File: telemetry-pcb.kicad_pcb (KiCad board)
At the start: 2 copper layers, 150 x 130 mm, 64 parts, among them CN1 12V_IN, CN10 CAN, CN11 CAN, CN12 CAN_12V_OUT, CN13 THERMO1, CN14 THERMO2, CN15 RS232, CN2 12V_OUT, CN3 12V_OUT, CN4 12V_OUT, CN5 12V_OUT, CN6 CAN, CN7 CAN, CN8 CAN, CN9 CAN, IC1 MAX31855K, IC2 MAX31855K, IC3 TCAN332DR, IC4 MAX3232CPWR, IC5 MCP2515-xSO, M1 MountingHole, M2 MountingHole, M3 MountingHole, M4 MountingHole, T1 TEST_12V, T2 TEST_3V3, T3 TEST_CAN, T4 GPIO_L, T5 GPIO_R, T6 TEST_RS232, Y1 8MHz

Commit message: small changes and gerber file for JLPCB
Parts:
- H1,H2: renamed from H1                  H2
- R3: value 68 -> 5.6
- R4: value 4.7 -> 5.6
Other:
- board text added: "12V"
- board text added: "2021-09-08"
- board text added: "Telemetry Module v1.0"

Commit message: added JLPCB gerber files
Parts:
- added G***: LOGO, Libraries:sm_logo, B.Cu at (80.0, 104.2)

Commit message: started on 1.1 redesign, schematic is done and PCB has just been started.
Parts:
- removed G***: LOGO, Libraries:sm_logo
- removed S2: AUX_BTN_1, TestPoint:TestPoint_2Pads_Pitch2.54mm_Drill0.8mm
- removed S4: AUX_BTN_3, TestPoint:TestPoint_2Pads_Pitch2.54mm_Drill0.8mm
- added C16: 0.1uF, Capacitor_SMD:C_0805_2012Metric, B.Cu at (-3.51, -37.9)
- added IC6: LSM6DSOTR, telemetry-pcb:LSM6DSOTR, B.Cu at (-24.7, -40.2)
- added J1: TTL, telemetry-pcb:molex_sl_1x04_horizontal, F.Cu at (63.3, 84.4)
- added R7: 120, Resistor_SMD:R_0805_2012Metric, B.Cu at (-21.6, 5.97)
- added R8: 10K, Resistor_SMD:R_0805_2012Metric, B.Cu at (1.41, -34.4)
- C1: value 0.1uF -> 47uF; footprint Capacitor_SMD:C_0805_2012Metric -> Capacitor_SMD:CP_Elec_6.3x5.4
- C10, C9: value 0.01uF -> 0.1uF; moved to B.Cu
- C11, C12, C15, C2, C3, C4, C5, C6, D1, IC2, R1, R3, R4, R5, R6: moved to B.Cu
- C13: value 10uF -> 0.1uF; footprint Capacitor_SMD:C_1206_3216Metric -> Capacitor_SMD:C_0805_2012Metric; moved to B.Cu
- C14: value 47uF -> 10uF; footprint Capacitor_SMD:CP_Elec_6.3x5.4 -> Capacitor_SMD:C_1206_3216Metric; moved to B.Cu
- C7, C8: value 0.1uF -> 0.01uF; moved to B.Cu
- CN1: value 12V_IN -> 12V_OUT; footprint Connector_Molex:Molex_Mega-Fit_76825-0004_2x02_P5.70mm_Horizontal -> Connector_Molex:Molex_Mega-Fit_76825-0004_1x02_P5.70mm_Horizontal
- CN10, CN11, CN6, CN8, CN9: footprint Conn_Molex_70553-0001:Molex-70553-0001-0-0-MFG -> telemetry-pcb:molex_sl_1x02_horizontal
- CN12: value CAN_12V_OUT -> CAN; footprint Connector_Molex:Molex_Mega-Fit_76825-0010_2x05_P5.70mm_Horizontal -> telemetry-pcb:molex_sl_1x02_horizontal
- CN13: value THERMO1 -> RS232; footprint Conn_Molex_70553-0002:Molex-70551-0002-0-0-0 -> telemetry-pcb:db-9
- CN14: value THERMO2 -> THERMO1; footprint Conn_Molex_70553-0002:Molex-70551-0002-0-0-0 -> telemetry-pcb:molex-sl-1x03-horizontal
- CN15: value RS232 -> THERMO2; footprint Libraries:DLS1XP5AK40X -> telemetry-pcb:molex-sl-1x03-horizontal
- CN2: value 12V_OUT -> 12V_IN; footprint Connector_Molex:Molex_Mega-Fit_76825-0004_1x02_P5.70mm_Horizontal -> Connector_Molex:Molex_Mega-Fit_76825-0004_2x02_P5.70mm_Horizontal
- CN7: value CAN -> CAN_12V_OUT; footprint Conn_Molex_70553-0001:Molex-70553-0001-0-0-MFG -> Connector_Molex:Molex_Mega-Fit_76825-0010_2x05_P5.70mm_Horizontal
- H1,H2: footprint Libraries:PCB_FeatherWing -> telemetry-pcb:Particle_boron
- IC1: value MAX31855K -> MAX3232CPWR; footprint Package_SO:SOIC-8-1EP_3.9x4.9mm_P1.27mm_EP2.29x3mm -> Package_SO:TSSOP-16_4.4x5mm_P0.65mm; moved to B.Cu
- IC3: value TCAN332DR -> MAX31855K; footprint Libraries:SOIC127P599X175-8N -> Package_SO:SOIC-8-1EP_3.9x4.9mm_P1.27mm_EP2.29x3mm; moved to B.Cu
- IC4: value MAX3232CPWR -> MCP2515-xSO; footprint Package_SO:TSSOP-16_4.4x5mm_P0.65mm -> Package_SO:SOIC-18W_7.5x11.6mm_P1.27mm; moved to B.Cu
- IC5: value MCP2515-xSO -> TCAN332DR; footprint Package_SO:SOIC-18W_7.5x11.6mm_P1.27mm -> Package_SO:SOIC-8-1EP_3.9x4.9mm_P1.27mm_EP2.29x3mm; moved to B.Cu
- R2: value 10K -> 120; moved to B.Cu
- S3: value AUX_BTN_2 -> LOG_BTN
- T1: value TEST_12V -> TEST_3V3
- T2: value TEST_3V3 -> TEST_12V
- moved C14 260.8 mm to (-30.5, -39.8), turned to 0 degrees
- moved D1 238.8 mm to (-36.1, -8.99), turned to 0 degrees
- moved R6 226.9 mm to (-21.6, 3.02)
- moved C9 225.4 mm to (-20.0, -39.8), turned to 0 degrees
- moved R3 224.5 mm to (-21.5, -19.3), turned to 0 degrees
- moved R4 223.1 mm to (-25.9, -19.3), turned to 0 degrees
- moved R5 204.1 mm to (-12.6, -16.3), turned to 0 degrees
- moved IC1 202.3 mm to (-11.7, -6.25), turned to 0 degrees
- moved C10 197.1 mm to (-15.5, -39.8), turned to 0 degrees
- moved C12 195.2 mm to (-11.1, -40.9), turned to 0 degrees
- moved C2 193.8 mm to (3.90, -4.46), turned to 0 degrees
- moved C11 184.6 mm to (-7.96, -37.9), turned to 0 degrees
- moved IC2 175.5 mm to (7.89, -20.0), turned to 0 degrees
- moved C5 171.5 mm to (-9.45, -11.0), turned to 0 degrees
- moved C6 170.9 mm to (-13.9, -11.0)
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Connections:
- C1 pad 1: +3V3 -> /VIN
- C10 pad 1: Net-(C10-Pad1) -> +3V3
- C10 pad 2: Net-(C10-Pad2) -> GND
- C13 pad 1: +3V3 -> GND
- C13 pad 2: GND -> +3V3
- C14 pad 1: /VIN -> +3V3
- C15 pad 1: GND -> +3V3
- C15 pad 2: +3V3 -> GND
- C2 pad 1: +3V3 -> Net-(C2-Pad1)
- C2 pad 2: GND -> Net-(C2-Pad2)
- C3 pad 2: GND -> Net-(C3-Pad2)
- C4 pad 1: GND -> Net-(C4-Pad1)
- C4 pad 2: Net-(C4-Pad2) -> GND
- C5 pad 1: Net-(C5-Pad1) -> GND
- C5 pad 2: Net-(C5-Pad2) -> +3V3
- C6 pad 1: Net-(C6-Pad1) -> GND
- C7 pad 1: GND -> Net-(C7-Pad1)
- C7 pad 2: +3V3 -> Net-(C7-Pad2)
- C8 pad 1: GND -> Net-(C8-Pad1)
- C8 pad 2: +3V3 -> Net-(C8-Pad2)
- C9 pad 1: Net-(C9-Pad1) -> +3V3
- C9 pad 2: Net-(C9-Pad2) -> GND
- CN1 pad 2: GND -> +12V
- CN10 pad 1: /CANL -> /Power & CAN Distribution/CANL
- CN10 pad 2: /CANH -> /Power & CAN Distribution/CANH
- CN11 pad 1: /CANL -> /Power & CAN Distribution/CANL
- CN11 pad 2: /CANH -> /Power & CAN Distribution/CANH
- CN12 pad 1: GND -> /Power & CAN Distribution/CANL
- CN12 pad 2: GND -> /Power & CAN Distribution/CANH
- CN13 pad 1: Net-(C9-Pad2) -> Net-(CN13-Pad1)
- CN13 pad 3: Net-(C9-Pad1) -> Net-(CN13-Pad3)
- CN14 pad 1: Net-(C10-Pad2) -> Net-(C7-Pad2)
- CN14 pad 3: Net-(C10-Pad1) -> Net-(C7-Pad1)
- CN15 pad 1: Net-(CN15-Pad1) -> Net-(C8-Pad2)
- CN15 pad 3: Net-(CN15-Pad3) -> Net-(C8-Pad1)
- CN2 pad 2: +12V -> GND
- CN6 pad 1: /CANL -> /Power & CAN Distribution/CANL
- CN6 pad 2: /CANH -> /Power & CAN Distribution/CANH
- CN7 pad 1: /CANL -> GND
- CN7 pad 2: /CANH -> GND
- CN8 pad 1: /CANL -> /Power & CAN Distribution/CANL
- CN8 pad 2: /CANH -> /Power & CAN Distribution/CANH
- CN9 pad 1: /CANL -> /Power & CAN Distribution/CANL
- CN9 pad 2: /CANH -> /Power & CAN Distribution/CANH
- F1 pad 1: Net-(CN1-Pad3) -> Net-(CN2-Pad3)
- IC1 pad 1: GND -> Net-(C2-Pad1)
- IC1 pad 2: Net-(C9-Pad1) -> Net-(C6-Pad2)
- IC1 pad 3: Net-(C9-Pad2) -> Net-(C2-Pad2)
- IC1 pad 4: +3V3 -> Net-(C3-Pad2)
- IC1 pad 5: /SCK -> Net-(C3-Pad1)
- IC1 pad 6: /A5 -> Net-(C4-Pad1)
- IC1 pad 7: /MI -> Net-(IC1-Pad7)
- IC1 pad 8: (no net) -> Net-(IC1-Pad8)
- IC1 pad 9: (no net) -> Net-(IC1-Pad9)
- IC2 pad 2: Net-(C10-Pad1) -> Net-(C7-Pad1)
- IC2 pad 3: Net-(C10-Pad2) -> Net-(C7-Pad2)
- IC2 pad 5: /SCK -> /MO
- IC2 pad 6: /A4 -> /A5
- IC3 pad 1: Net-(IC3-Pad1) -> GND
- IC3 pad 2: GND -> Net-(C8-Pad1)
- IC3 pad 3: +3V3 -> Net-(C8-Pad2)
- IC3 pad 4: Net-(IC3-Pad4) -> +3V3
- IC3 pad 5: (no net) -> /MO
- IC3 pad 6: /CANL -> /A4
- IC3 pad 7: /CANH -> /MI
- IC4 pad 1: Net-(C6-Pad1) -> Net-(IC4-Pad1)
- IC4 pad 11: /TX -> Net-(IC4-Pad11)
- IC4 pad 12: /RX -> /D6
- IC4 pad 13: Net-(CN15-Pad3) -> /SCK1
- IC4 pad 14: Net-(CN15-Pad2) -> /MO1
- IC4 pad 15: GND -> /MI1
- IC4 pad 16: +3V3 -> /D5
- IC4 pad 2: Net-(C4-Pad2) -> Net-(IC4-Pad2)
- IC4 pad 3: Net-(C6-Pad2) -> Net-(IC4-Pad3)
- IC4 pad 4: Net-(C5-Pad2) -> Net-(IC4-Pad4)
- IC4 pad 5: Net-(C5-Pad1) -> Net-(IC4-Pad5)
- IC4 pad 6: Net-(C3-Pad1) -> Net-(IC4-Pad6)
- IC4 pad 7: Net-(IC4-Pad7) -> Net-(C11-Pad1)
- IC4 pad 8: Net-(IC4-Pad8) -> Net-(C12-Pad1)
- IC4 pad 9: Net-(IC4-Pad9) -> GND
- IC5 pad 1: Net-(IC3-Pad1) -> Net-(IC4-Pad1)
- IC5 pad 2: Net-(IC3-Pad4) -> GND
- IC5 pad 3: Net-(IC5-Pad3) -> +3V3
- IC5 pad 4: Net-(IC5-Pad4) -> Net-(IC4-Pad2)
- IC5 pad 5: Net-(IC5-Pad5) -> (no net)
- IC5 pad 6: Net-(IC5-Pad6) -> /Power & CAN Distribution/CANL
- IC5 pad 7: Net-(C11-Pad1) -> /Power & CAN Distribution/CANH
- IC5 pad 8: Net-(C12-Pad1) -> (no net)
- IC5 pad 9: GND -> (no net)
- R1 pad 1: Net-(R1-Pad1) -> GND
- R1 pad 2: /CANL -> /A1
- R2 pad 1: Net-(IC5-Pad17) -> /A1
- R2 pad 2: +3V3 -> /VIN
- R5 pad 1: /A0 -> Net-(L4-Pad2)
- R5 pad 2: Net-(L4-Pad2) -> /A0
- R6 pad 1: /VIN -> Net-(L1-Pad2)
- R6 pad 2: Net-(L1-Pad2) -> +12V
- S1 pad 1: /CANH -> Net-(R7-Pad1)
- S1 pad 2: Net-(R1-Pad1) -> /Power & CAN Distribution/CANL
- T1 pad 1: +12V -> +3V3
- T2 pad 1: +3V3 -> +12V
- T3 pad 1: /CANL -> /Power & CAN Distribution/CANL
- T3 pad 2: /CANH -> /Power & CAN Distribution/CANH
- T6 pad 1: Net-(CN15-Pad2) -> Net-(CN13-Pad2)
- T6 pad 2: Net-(CN15-Pad3) -> Net-(CN13-Pad3)
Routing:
- net +3V3: track 241.1 -> 0.00 mm, vias 8 -> 0
- net /CANH: track 201.2 -> 0.00 mm, vias 3 -> 0
- net /CANL: track 193.6 -> 0.00 mm, vias 2 -> 0
- net GND: track 160.7 -> 0.00 mm, vias 4 -> 0
- net /SDA: track 120.5 -> 0.00 mm
- net /SCL: track 114.5 -> 0.00 mm, vias 1 -> 0
- net /A3: track 99.6 -> 0.00 mm
- net /A2: track 96.1 -> 0.00 mm
- net /A1: track 92.5 -> 0.00 mm
- net /D6: track 66.3 -> 0.00 mm, vias 1 -> 0
- net /D5: track 56.3 -> 0.00 mm
- net /MI1: track 53.2 -> 0.00 mm
- net /MO1: track 50.1 -> 0.00 mm
- net Net-(L2-Pad2): track 49.1 -> 0.00 mm
- net /A0: track 47.8 -> 0.00 mm
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- removed copper zone on F.Cu, net +12V
- removed copper zone on B.Cu, net GND
- removed copper zone on F.Cu, net GND
- removed copper zone on F.Cu, net Net-(CN1-Pad3)
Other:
- board size 150 x 130 mm -> 150 x 100 mm
- board text removed: "12V"
- board text removed: "12V+"
- board text removed: "12V_OUT"
- board text removed: "2021-09-08"
- board text removed: "3V3"
- board text removed: "CAN"
- board text removed: "CELL ANTENNA"
- board text removed: "GND"
- board text removed: "H"
- board text removed: "L"
- board text removed: "RX"
- board text removed: "TX"
- board text removed: "Telemetry Module v1.0"

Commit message: finished schematic and PCB layout for 1.1 board
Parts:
- removed CN10, CN11, CN12, CN9: CAN, telemetry-pcb:molex_sl_1x02_horizontal
- removed the CN3 at (123.7, 103.7)
- removed the CN5 at (159.3, 103.7)
- removed the CN6 at (65.3, 27.0)
- removed the R6 at (-21.6, 3.02)
- removed S3: LOG_BTN, TestPoint:TestPoint_2Pads_Pitch2.54mm_Drill0.8mm
- removed the T2 at (148.6, 81.3)
- removed the T3 at (114.1, 40.7)
- added J2: Header 02x03, Connector_PinHeader_2.54mm:PinHeader_2x03_P2.54mm_Horizontal, F.Cu at (82.6, 80.8)
- added Q1: IF-D92, telemetry-pcb:IF-D92, F.Cu at (173.5, 66.6)
- added R3: 10K, Resistor_SMD:R_0805_2012Metric, B.Cu at (186.7, 98.6)
- added R9: 120, Resistor_SMD:R_0805_2012Metric, B.Cu at (133.4, 108.8)
- added S2: CAN_TERM, Button_Switch_THT:SW_DIP_SPSTx01_Piano_10.8x4.1mm_W7.62mm_P2.54mm, F.Cu at (135.9, 121.0)
- added T1: TEST_12V, TestPoint:TestPoint_2Pads_Pitch2.54mm_Drill0.8mm, F.Cu at (76.0, 109.3)
- added T6: TEST_CAN, TestPoint:TestPoint_2Pads_Pitch2.54mm_Drill0.8mm, F.Cu at (73.4, 114.4)
- CN1: value 12V_OUT -> 12V; footprint Connector_Molex:Molex_Mega-Fit_76825-0004_1x02_P5.70mm_Horizontal -> telemetry-pcb:molex_sl_1x04_horizontal
- CN2: value 12V_IN -> 12V; footprint Connector_Molex:Molex_Mega-Fit_76825-0004_2x02_P5.70mm_Horizontal -> telemetry-pcb:molex_sl_1x04_horizontal
- CN4: value 12V_OUT -> UART; footprint Connector_Molex:Molex_Mega-Fit_76825-0004_1x02_P5.70mm_Horizontal -> telemetry-pcb:Molex-70551-0004-0
- CN7: value CAN_12V_OUT -> CAN; footprint Connector_Molex:Molex_Mega-Fit_76825-0010_2x05_P5.70mm_Horizontal -> telemetry-pcb:molex_sl_1x02_horizontal
- D1: value 1A 50v -> 2A 50v; moved to F.Cu
- F1: value 25A -> 1A; footprint Fuse:Fuseholder_Blade_Mini_Keystone_3568 -> telemetry-pcb:0154001.DRL
- G1: renamed from H3; footprint Connector_PinSocket_2.54mm:PinSocket_1x08_P2.54mm_Vertical -> telemetry-pcb:Sparkfun GPS
- J1: value TTL -> Header 02x02; footprint telemetry-pcb:molex_sl_1x04_horizontal -> Connector_PinHeader_2.54mm:PinHeader_2x02_P2.54mm_Horizontal
- R1: value 120 -> 2.2K
- R2: value 120 -> 560
- R4: renamed from R5; moved to F.Cu
- R5: renamed from R4; moved to F.Cu
- R6: renamed from R3; moved to F.Cu
- R7: value 120 -> 10K
- S1: value CAN_TERM -> LOG; footprint Button_Switch_THT:SW_DIP_SPSTx01_Piano_10.8x4.1mm_W7.62mm_P2.54mm -> Button_Switch_THT:SW_PUSH_6mm_H13mm
- moved C14 253.8 mm to (176.0, 107.8), turned to 90 degrees
- moved C13 222.2 mm to (181.6, 108.3), turned to 270 degrees
- moved R1 221.0 mm to (181.6, 98.6), turned to 90 degrees
- moved R8 220.7 mm to (175.5, 101.2), turned to 270 degrees
- moved IC6 220.2 mm to (144.6, 100.6)
- moved C11 217.6 mm to (153.7, 107.8), turned to 90 degrees
- moved C12 217.2 mm to (153.7, 100.6), turned to 270 degrees
- moved R7 213.3 mm to (182.1, 69.2)
- moved C15 212.1 mm to (147.6, 104.7)
- moved IC4 211.9 mm to (166.4, 104.2)
- moved D1 206.1 mm to (137.4, 102.2), turned to 180 degrees
- moved R6 202.2 mm to (157.8, 74.2), turned to 90 degrees
- moved R5 201.2 mm to (152.2, 74.2), turned to 270 degrees
- moved IC5 195.1 mm to (121.2, 105.2), turned to 180 degrees
- moved C16 193.4 mm to (128.8, 103.2), turned to 270 degrees
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- renumbered CN13 to CN3, CN14 to CN5, CN15 to CN6, H1,H2 to H1, L4 to L2, L2 to L4, T4 to T2, T5 to T3, T1 to T4, T6 to T5
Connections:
- CN1 pad 2: +12V -> GND
- CN2 pad 3: Net-(CN2-Pad3) -> Net-(CN1-Pad3)
- CN2 pad 4: Net-(CN2-Pad3) -> Net-(CN1-Pad3)
- CN3 pad 5: Net-(CN13-Pad5) -> GND
- CN4 pad 2: +12V -> Net-(CN4-Pad2)
- CN7 pad 1: GND -> Net-(CN7-Pad1)
- CN7 pad 2: GND -> Net-(CN7-Pad2)
- CN8 pad 1: /Power & CAN Distribution/CANL -> Net-(CN7-Pad1)
- CN8 pad 2: /Power & CAN Distribution/CANH -> Net-(CN7-Pad2)
- D1 pad 2: +12V -> Net-(D1-Pad2)
- F1 pad 1: Net-(CN2-Pad3) -> Net-(CN1-Pad3)
- F1 pad 2: +12V -> Net-(D1-Pad2)
- IC1 pad 11: /TX -> Net-(IC1-Pad11)
- IC1 pad 12: /RX -> Net-(IC1-Pad12)
- IC2 pad 5: /MO -> /SCK
- IC3 pad 5: /MO -> /SCK
- IC5 pad 6: /Power & CAN Distribution/CANL -> Net-(CN7-Pad1)
- IC5 pad 7: /Power & CAN Distribution/CANH -> Net-(CN7-Pad2)
- IC6 pad 13: /MO -> /SCK
- IC6 pad 14: /SCK -> /MO
- J1 pad 1: /TX -> Net-(IC1-Pad11)
- J1 pad 3: /RX -> Net-(CN4-Pad4)
- J1 pad 4: /RX -> /TX
- R2 pad 1: /A1 -> Net-(D1-Pad2)
- R2 pad 2: /VIN -> Net-(L1-Pad2)
- R7 pad 1: Net-(R7-Pad1) -> Net-(Q1-Pad2)
- R7 pad 2: /Power & CAN Distribution/CANH -> GND
- S1 pad 1: Net-(R7-Pad1) -> GND
- S1 pad 2: /Power & CAN Distribution/CANL -> /A2
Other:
- board size 150 x 100 mm -> 120 x 70 mm

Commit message: routed all
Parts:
- R2: moved to F.Cu
- T2: footprint Connector_PinSocket_2.54mm:PinSocket_1x15_P2.54mm_Vertical -> telemetry-pcb:Boron_Pins_L
- T3: footprint Connector_PinSocket_2.54mm:PinSocket_1x12_P2.54mm_Vertical -> telemetry-pcb:Boron_Pins_R
- moved C1 17.3 mm to (135.4, 101.7)
- moved R2 16.1 mm to (127.3, 74.7), turned to 270 degrees
- moved D1 15.9 mm to (122.7, 96.1)
- moved C15 3.09 mm to (144.6, 105.2)
- moved IC4 1.14 mm to (165.4, 103.7)
- moved L1 1.14 mm to (127.3, 79.8), turned to 90 degrees
- moved C13 1.14 mm to (180.6, 107.8)
- moved C14 1.02 mm to (175.0, 107.8)
- moved C4 0.07 mm to (135.4, 78.7), turned to 270 degrees
- turned F1 to 0 degrees
- turned IC2 to 270 degrees
- turned IC3 to 270 degrees
- turned R6 to 270 degrees
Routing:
- net GND: track 0.00 -> 157.0 mm, vias 0 -> 24
- net Net-(J2-Pad5): track 0.00 -> 109.2 mm
- net Net-(IC1-Pad11): track 0.00 -> 103.3 mm
- net /VIN: track 0.00 -> 102.2 mm
- net /SCK: track 0.00 -> 97.4 mm, vias 0 -> 2
- net +3V3: track 0.00 -> 97.1 mm, vias 0 -> 12
- net /RX: track 0.00 -> 93.5 mm, vias 0 -> 4
- net /MI: track 0.00 -> 90.1 mm, vias 0 -> 4
- net Net-(IC1-Pad12): track 0.00 -> 88.8 mm
- net Net-(D1-Pad2): track 0.00 -> 82.1 mm
- net /TX: track 0.00 -> 79.0 mm, vias 0 -> 3
- net /A4: track 0.00 -> 79.0 mm, vias 0 -> 2
- net /A5: track 0.00 -> 78.3 mm
- net Net-(CN7-Pad2): track 0.00 -> 74.7 mm
- net Net-(CN7-Pad1): track 0.00 -> 71.4 mm
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- added copper zone on F.Cu, net +3V3
- added copper zone on B.Cu, net GND
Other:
- net class Default: clearance 0.2 -> 0.127
- rule trace_clearance: 0.2 -> 0.127
- rule trace_min: 0.2 -> 0.127

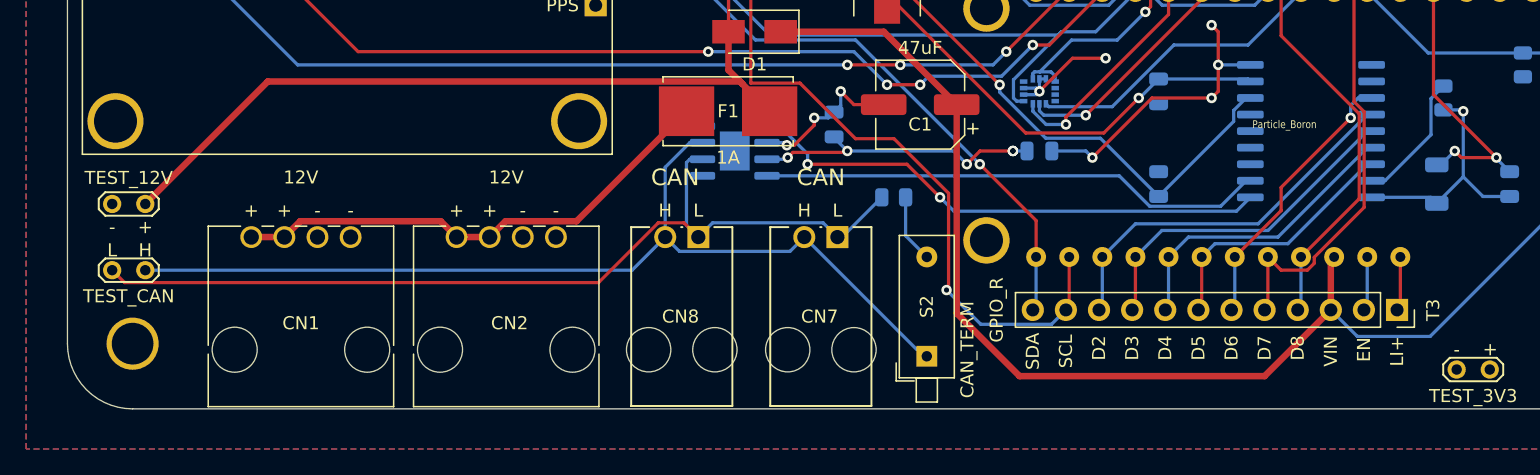
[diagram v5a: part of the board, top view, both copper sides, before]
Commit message: removes one power port, changes CAN switch to jumper
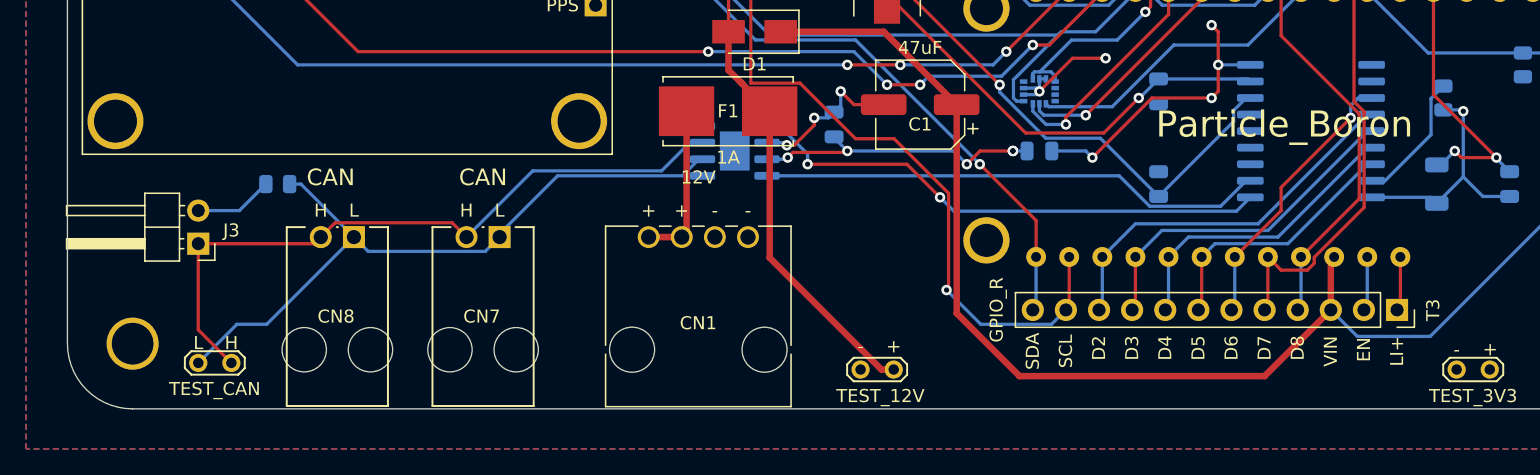
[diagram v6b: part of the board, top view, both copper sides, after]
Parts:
- removed CN2: 12V, telemetry-pcb:molex_sl_1x04_horizontal
- removed S2: CAN_TERM, Button_Switch_THT:SW_DIP_SPSTx01_Piano_10.8x4.1mm_W7.62mm_P2.54mm
- added J3: CAN_TERM, Connector_PinHeader_2.54mm:PinHeader_1x02_P2.54mm_Horizontal, F.Cu at (80.0, 112.3)
- J1: value Header 02x02 -> TX_SEL
- J2: value Header 02x03 -> RX_SEL
- moved T1 58.8 mm to (133.4, 122.0)
- moved R9 47.3 mm to (86.1, 107.8), turned to 0 degrees
- moved CN1 30.5 mm to (122.2, 111.8)
- moved CN8 26.4 mm to (90.7, 117.9)
- moved CN7 25.9 mm to (101.9, 117.9)
- moved T6 9.71 mm to (80.0, 121.5)
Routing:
- net Net-(CN1-Pad3): track 38.4 -> 12.3 mm
- net Net-(D1-Pad2): track 82.1 -> 56.9 mm
- net Net-(CN7-Pad2): track 74.7 -> 53.0 mm
- net Net-(CN7-Pad1): track 71.4 -> 54.1 mm
- net Net-(J3-Pad2): track 5.25 -> 6.03 mm

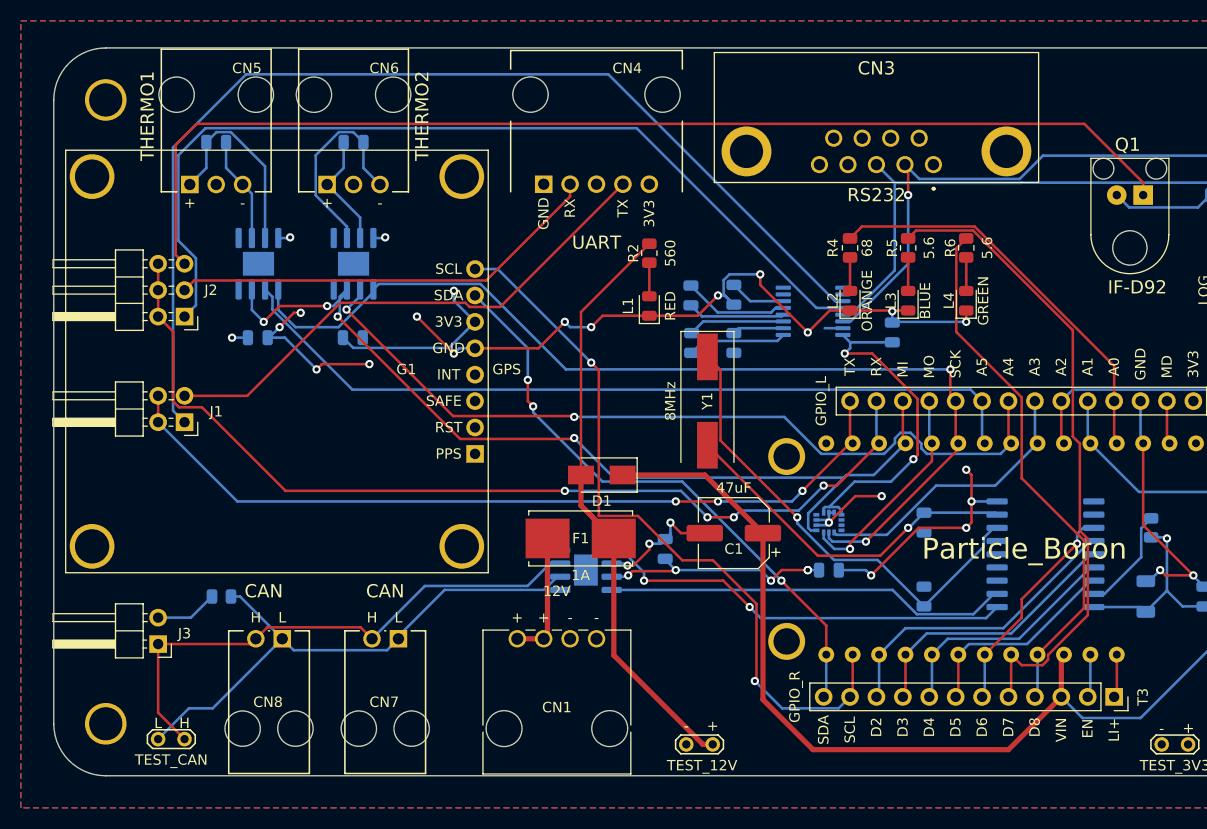
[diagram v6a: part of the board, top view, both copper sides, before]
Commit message: updates PCB to move serial headers next to serial ports, CAN header next to CAN ports
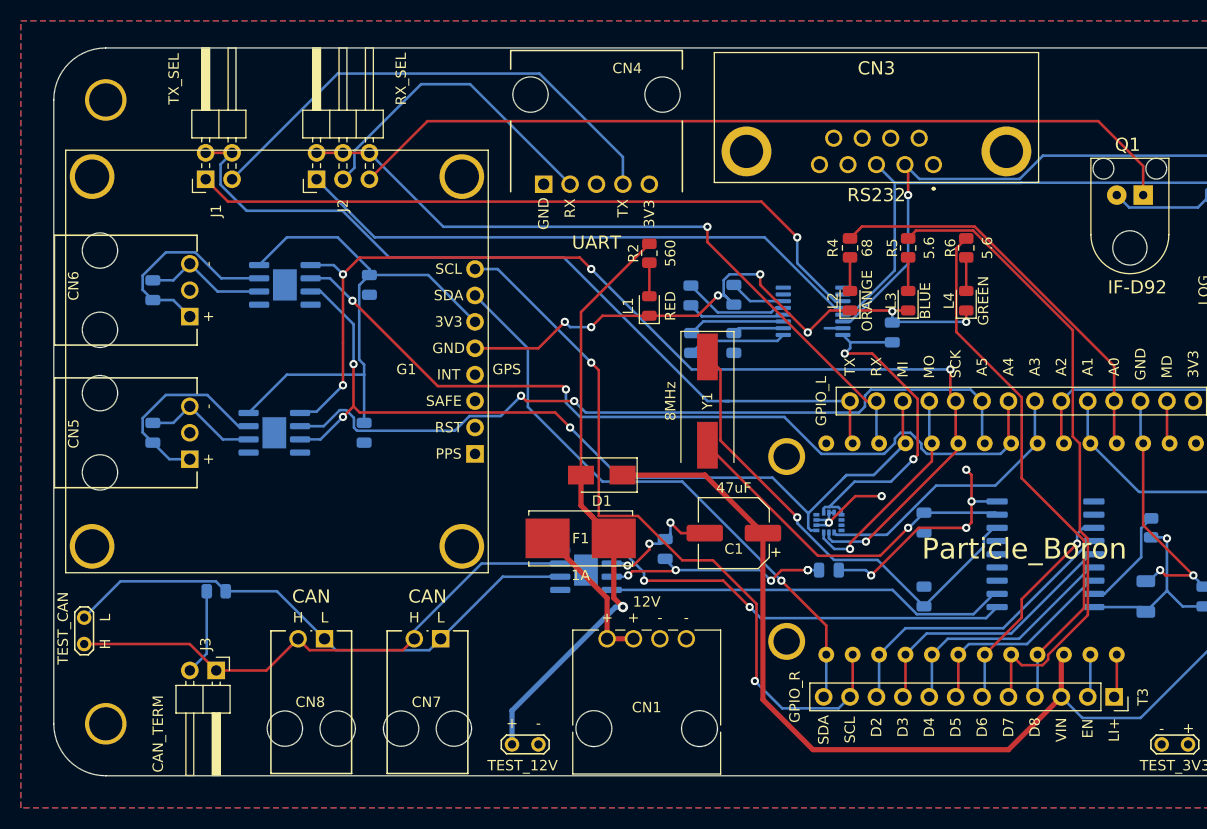
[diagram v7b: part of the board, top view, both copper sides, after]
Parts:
- moved CN5 31.2 mm to (77.0, 92.0), turned to 270 degrees
- moved C7 28.6 mm to (79.5, 92.0), turned to 270 degrees
- moved CN6 27.2 mm to (77.0, 78.3), turned to 270 degrees
- moved C8 24.0 mm to (79.5, 78.3), turned to 270 degrees
- moved J1 23.5 mm to (84.6, 67.6), turned to 90 degrees
- moved T1 19.3 mm to (114.1, 122.0), turned to 0 degrees
- moved J2 18.3 mm to (95.3, 67.6), turned to 90 degrees
- moved IC2 16.3 mm to (91.2, 92.0), turned to 0 degrees
- moved T6 13.7 mm to (72.9, 109.8), turned to 270 degrees
- moved C9 11.9 mm to (100.4, 77.8), turned to 270 degrees
- moved C10 9.21 mm to (99.8, 92.0), turned to 270 degrees
- moved CN1 8.64 mm to (130.8, 111.8)
- moved IC3 6.91 mm to (92.2, 77.8), turned to 0 degrees
- moved J3 6.14 mm to (85.6, 114.9), turned to 270 degrees
- moved CN7 4.06 mm to (105.9, 117.9)
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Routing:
- net Net-(IC1-Pad11): track 103.3 -> 67.6 mm, vias 0 -> 1
- net Net-(IC1-Pad12): track 88.8 -> 55.7 mm
- net +3V3: track 97.1 -> 128.3 mm, vias 12 -> 8
- net Net-(J2-Pad5): track 109.2 -> 81.3 mm
- net /RX: track 93.5 -> 68.8 mm, vias 4 -> 1
- net GND: track 157.0 -> 134.3 mm, vias 24 -> 18
- net Net-(CN4-Pad2): track 42.0 -> 30.6 mm
- net /SCK: track 97.4 -> 107.7 mm, vias 2 -> 5
- net Net-(C8-Pad2): track 11.2 -> 20.1 mm
- net Net-(C8-Pad1): track 19.8 -> 12.0 mm
- net /MI: track 90.1 -> 86.7 mm, vias 4 -> 3
- net Net-(CN4-Pad4): track 50.9 -> 47.7 mm
- net /A4: track 79.0 -> 81.9 mm
- net /A5: track 78.3 -> 75.8 mm, vias 0 -> 2
- net Net-(J3-Pad2): track 6.03 -> 8.29 mm
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
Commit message: Updates BOM
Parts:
- R2: value 560 -> 680
- R5: value 5.6 -> 6.8
- R6: value 5.6 -> 150
- renumbered CN8 to CN2, G1 to H2
